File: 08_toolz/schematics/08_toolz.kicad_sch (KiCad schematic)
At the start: 22 parts, among them J1 Eurorack 10 pin power connect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, J2 In, J3 CV out, SW1 LIN/LOG, SW2 INV, U1 TL074

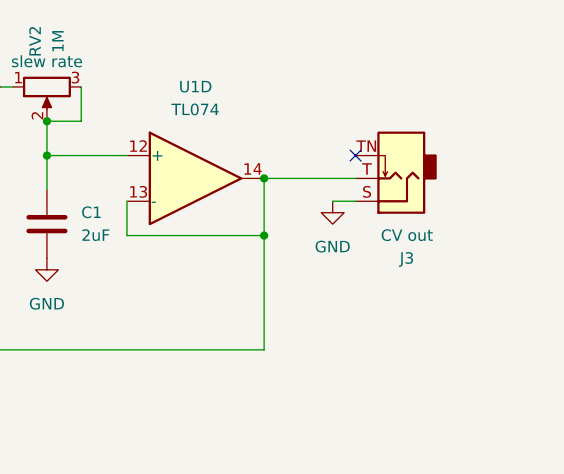
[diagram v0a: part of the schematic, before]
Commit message: fixed 08 stripboard
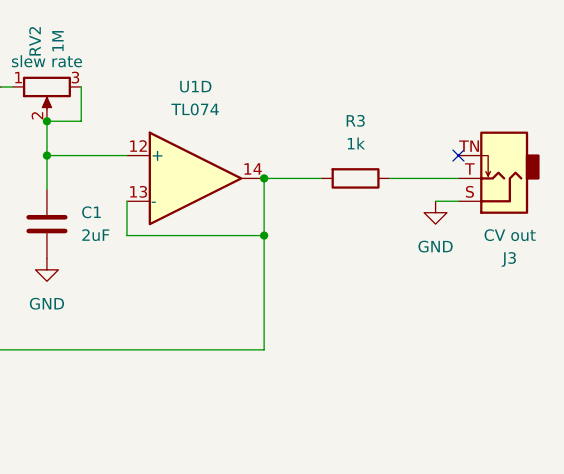
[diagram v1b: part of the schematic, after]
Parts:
- added R3: 1k, Resistor_THT:R_Axial_DIN0207_L6.3mm_D2.5mm_P10.16mm_Horizontal, symbol Device:R
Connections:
- net at SW1.3 (C), U1.13 (-), U1.14: now also R3.2; no longer J3.T
- new net: J3.T, R3.1
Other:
- moved on the sheet: J3
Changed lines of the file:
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@@
 	)
 	(no_connect
-		(at 196.85 68.58)
+		(at 208.28 68.58)
 	)
 	(wire
@@
 	(wire
 		(pts
+			(xy 200.66 71.12) (xy 208.28 71.12)
+		)
+		(stroke
+			(width 0)
+			(type default)
+		)
+	)
+	(wire
+		(pts
 			(xy 69.85 168.91) (xy 73.66 168.91)
 		)
@@
 	(wire
 		(pts
-			(xy 196.85 73.66) (xy 194.31 73.66)
+			(xy 208.28 73.66) (xy 205.74 73.66)
 		)
 		(stroke
@@
 	(wire
 		(pts
-			(xy 186.69 71.12) (xy 196.85 71.12)
+			(xy 186.69 71.12) (xy 193.04 71.12)
 		)
 		(stroke
@@
 	)
 	(symbol
+		(lib_id "Device:R")
+		(at 196.85 71.12 270)
+		(unit 1)
+		(exclude_from_sim no)
+		(in_bom yes)
+		(on_board yes)
+		(dnp no)
+		(fields_autoplaced yes)
+		(property "Reference" "R3"
+			(at 196.85 64.77 90)
+			(effects
+				(font
+					(size 1.27 1.27)
+				)
+			)
+		)
+		(property "Value" "1k"
+			(at 196.85 67.31 90)
+			(effects
+				(font
+					(size 1.27 1.27)
+				)
+			)
+		)
+		(property "Footprint" "Resistor_THT:R_Axial_DIN0207_L6.3mm_D2.5mm_P10.16mm_Horizontal"
+			(at 196.85 69.342 90)
+			(effects
+				(font
+					(size 1.27 1.27)
+				)
+				(hide yes)
+			)
+		)
+		(property "Datasheet" "~"
+			(at 196.85 71.12 0)
+			(effects
+				(font
+					(size 1.27 1.27)
+				)
+				(hide yes)
+			)
+		)
+		(property "Description" ""
+			(at 196.85 71.12 0)
+			(effects
+				(font
+					(size 1.27 1.27)
+				)
+				(hide yes)
+			)
+		)
+		(pin "1"
+		)
+		(pin "2"
+		)
+		(instances
+			(project "08_toolz"
+				(path "/8396c6e8-a50d-4664-b133-cb705f5400f1"
+					(reference "R3")
+					(unit 1)
+				)
+			)
+		)
+	)
+	(symbol
 		(lib_id "power:+12V")
 		(at 41.91 64.77 0)
@@
 	(symbol
 		(lib_id "Connector_Audio:AudioJack2_SwitchT")
-		(at 201.93 71.12 180)
+		(at 213.36 71.12 180)
 		(unit 1)
 		(exclude_from_sim no)
@@
 		(dnp no)
 		(property "Reference" "J3"
-			(at 202.565 80.01 0)
+			(at 213.995 80.01 0)
 			(effects
 				(font
@@
 		)
 		(property "Value" "CV out"
-			(at 202.565 77.47 0)
+			(at 213.995 77.47 0)
 			(effects
 				(font
@@
 		)
 		(property "Footprint" "Connector_Audio:Jack_6.35mm_Neutrik_NJ5FD-V_Vertical"
-			(at 201.93 71.12 0)
+			(at 213.36 71.12 0)
 			(effects
 				(font
@@
 		)
 		(property "Datasheet" "~"
-			(at 201.93 71.12 0)
+			(at 213.36 71.12 0)
 			(effects
 				(font
@@
 		)
 		(property "Description" "Audio Jack, 2 Poles (Mono / TS), Switched T Pole (Normalling)"
-			(at 201.93 71.12 0)
+			(at 213.36 71.12 0)
 			(effects
 				(font
@@
 	(symbol
 		(lib_id "power:GND")
-		(at 194.31 73.66 0)
+		(at 205.74 73.66 0)
 		(unit 1)
 		(exclude_from_sim no)
@@
 		(fields_autoplaced yes)
 		(property "Reference" "#PWR08"
-			(at 194.31 80.01 0)
+			(at 205.74 80.01 0)
 			(effects
 				(font
@@
 		)
 		(property "Value" "GND"
-			(at 194.31 78.74 0)
+			(at 205.74 78.74 0)
 			(effects
 				(font
@@
 		)
 		(property "Footprint" ""
-			(at 194.31 73.66 0)
+			(at 205.74 73.66 0)
 			(effects
 				(font
@@
 		)
 		(property "Datasheet" ""
-			(at 194.31 73.66 0)
+			(at 205.74 73.66 0)
 			(effects
 				(font
@@
 		)
 		(property "Description" "Power symbol creates a global label with name \"GND\" , ground"
-			(at 194.31 73.66 0)
+			(at 205.74 73.66 0)
 			(effects
 				(font
